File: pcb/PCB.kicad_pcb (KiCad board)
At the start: 4 copper layers, 145 x 73 mm, 284 parts, among them J1 TC2030, J2 JST B24B-PADSS-F, J3 TC2030, J4 JST B04B-XASK, U1 AMS1117-3.3, U17 ESD224DQA, U18 ESD224DQA, U19 ESD224DQA, U2 ADP2303ARDZ-5.0, U20 ESD224DQA, U3 74HCT541, U4 STM32F103C8T6, U5 SN65HVD230, U6 ADP2303ARDZ-5.0, Y1 8MHz

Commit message: added br24 changes
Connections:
- D102 pad 4: LED_DATA_6 -> /WS2812/Digit 4/DATA_OUT
- D112 pad 2: /WS2812/Digit 4/DATA_OUT -> LED_DATA_6
- D117 pad 4: LED_DATA_7 -> /WS2812/Digit 5/DATA_OUT
- D127 pad 2: /WS2812/Digit 5/DATA_OUT -> LED_DATA_7
- D42 pad 4: LED_DATA_3 -> /WS2812/Digit 1/DATA_OUT
- D52 pad 2: /WS2812/Digit 1/DATA_OUT -> LED_DATA_3
- D57 pad 4: LED_DATA_2 -> /WS2812/Digit 0/DATA_OUT
- D67 pad 2: /WS2812/Digit 0/DATA_OUT -> LED_DATA_2
- D72 pad 4: LED_DATA_4 -> /WS2812/Digit 2/DATA_OUT
- D82 pad 2: /WS2812/Digit 2/DATA_OUT -> LED_DATA_4
- D87 pad 4: LED_DATA_5 -> /WS2812/Digit 3/DATA_OUT
- D97 pad 2: /WS2812/Digit 3/DATA_OUT -> LED_DATA_5
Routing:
- net LED_DATA_4: track 57.2 -> 93.3 mm
- net LED_DATA_7: track 116.1 -> 151.3 mm
- net LED_DATA_5: track 76.8 -> 111.7 mm
- net LED_DATA_6: track 96.3 -> 128.0 mm
- net LED_DATA_2: track 17.3 -> 38.4 mm
- net LED_DATA_3: track 37.5 -> 58.6 mm

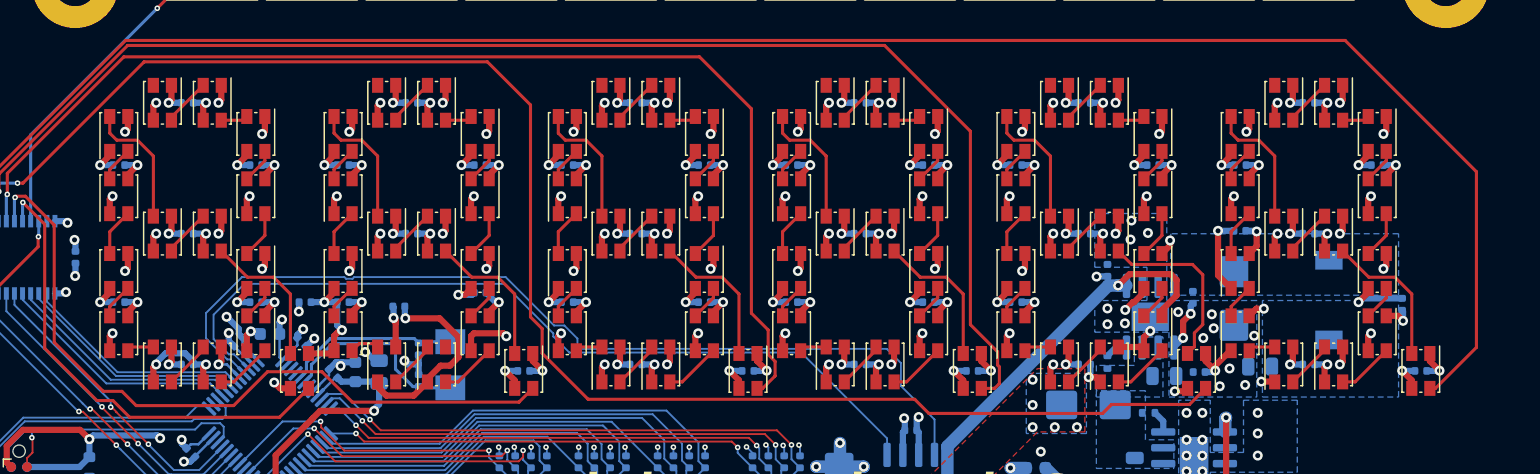
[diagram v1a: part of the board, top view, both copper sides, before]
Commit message: LED Footprints fixed
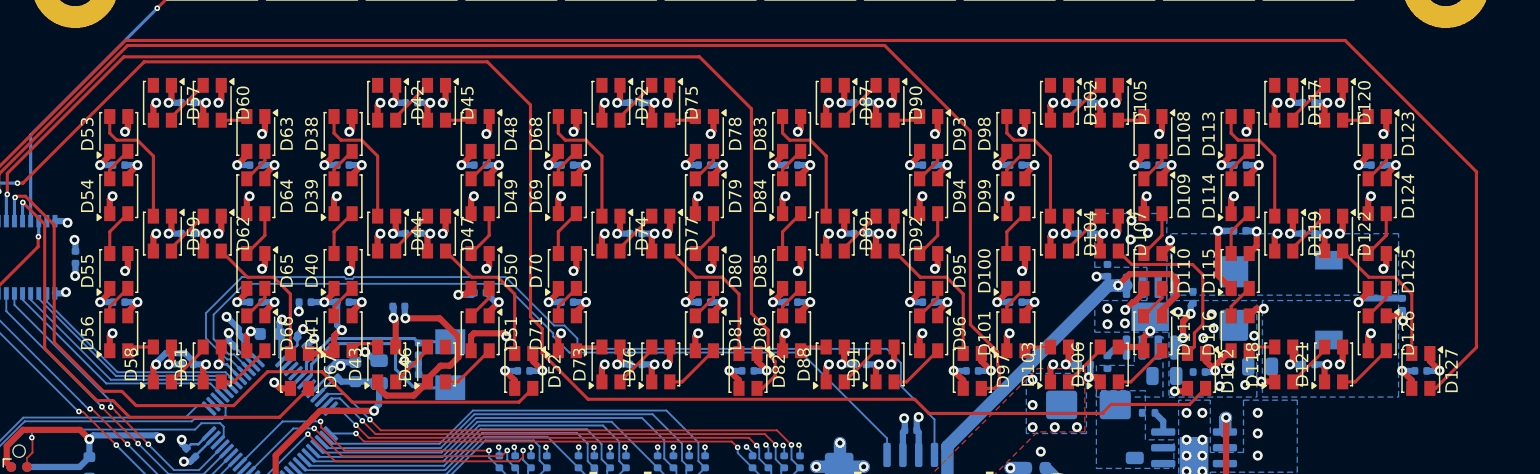
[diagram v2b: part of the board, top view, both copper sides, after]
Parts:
- D10, D11, D12, D13, D14, D15, D16, D17, D18, D19, D20, D21, D22, D24, D25, D26, D27, D28, D29, D3, D30, D31, D32, D33, D34, D35, D36, D37, D4, D8, D9, DD23: value WS2812B -> WS2812B-5x5
- D100, D101, D102, D103, D104, D105, D106, D107, D108, D109, D110, D111, D112, D113, D114, D115, D116, D117, D118, D119, D120, D121, D122, D123, D124, D125, D126, D127, D38, D39, D40, D41, D42, D43, D44, D45, D46, D47, D48, D49, D50, D51, D52, D53, D54, D55, D56, D57, D58, D59, D60, D61, D62, D63, D64, D65, D66, D67, D68, D69, D70, D71, D72, D73, D74, D75, D76, D77, D78, D79, D80, D81, D82, D83, D84, D85, D86, D87, D88, D89, D90, D91, D92, D93, D94, D95, D96, D97, D98, D99: footprint XL-3528RGBW-WS2812B:XL-3528RGBW-WS2812B -> LED_SMD:LED_Kingbright_AAA3528ESGCT
